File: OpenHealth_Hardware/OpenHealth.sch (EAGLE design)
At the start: 17 parts

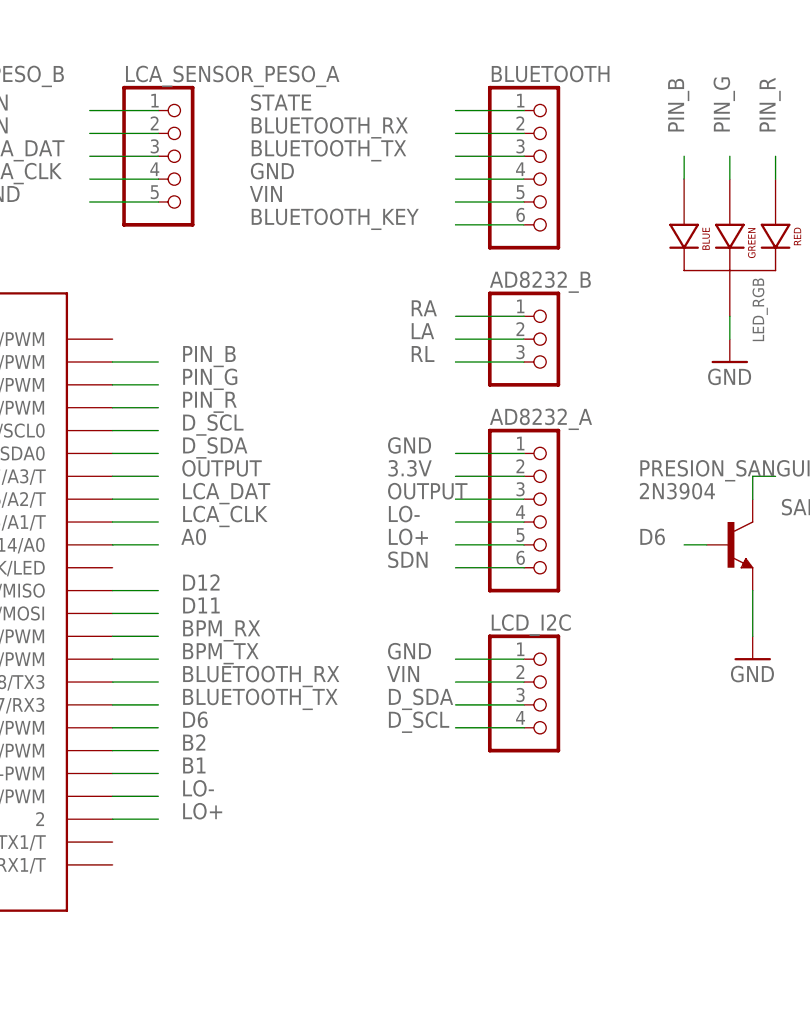
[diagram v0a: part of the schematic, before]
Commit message: Creacion del PCB board y simulacion de los componentes que iran abordo del circuito, PCB board sin enrutar.
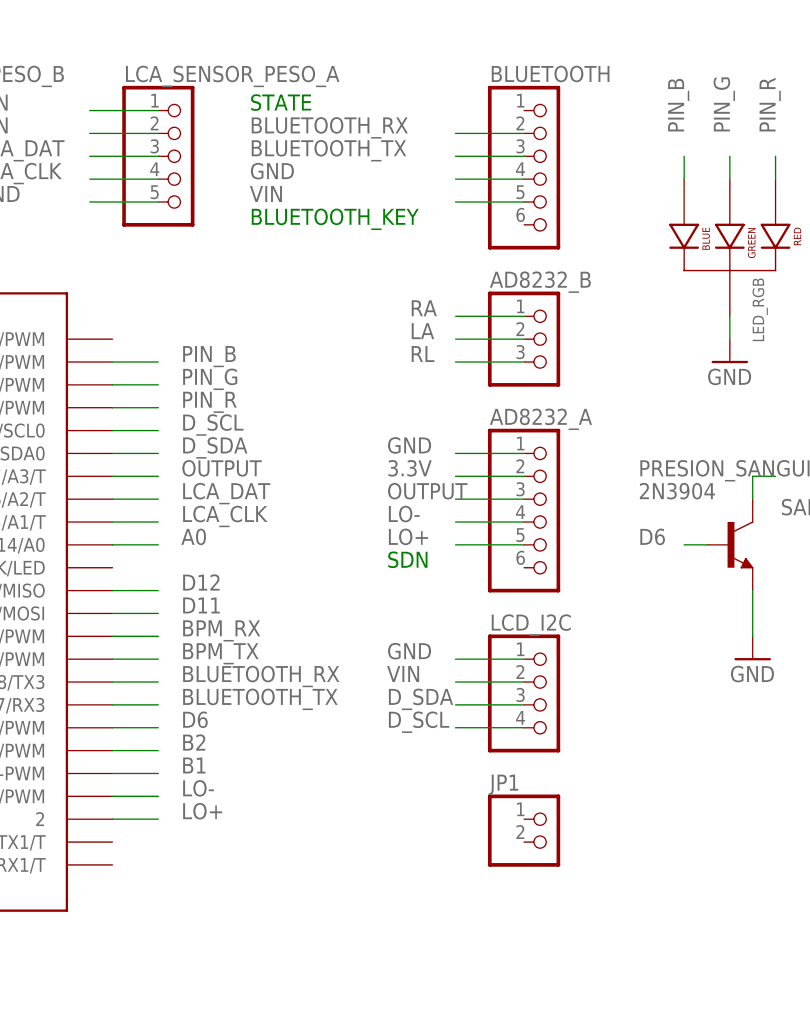
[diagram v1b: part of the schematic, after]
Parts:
- added JP1: (no value), pinhead:PINHD-1X2
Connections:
- removed net BLUETOOTH_KEY: BLUETOOTH.6
- removed net SDN: AD8232_A.6
- removed net STATE: BLUETOOTH.1
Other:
- note added: "BLUETOOTH_KEY"
- note added: "SDN"
- note added: "STATE"
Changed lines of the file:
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@@
 <part name="PRESION_SANGUIENA" library="transistor" deviceset="2N3904" device=""/>
 <part name="GND5" library="supply1" deviceset="GND" device=""/>
+<part name="JP1" library="pinhead" deviceset="PINHD-1X2" device=""/>
 </parts>
 <sheets>
 <sheet>
 <plain>
+<text x="5.08" y="137.16" size="1.778" layer="91">BLUETOOTH_KEY</text>
+<text x="5.08" y="149.86" size="1.778" layer="91">STATE</text>
+<text x="20.32" y="99.06" size="1.778" layer="91">SDN</text>
 </plain>
 <instances>
@@
 <instance part="PRESION_SANGUIENA" gate="G1" x="58.42" y="101.6"/>
 <instance part="GND5" gate="1" x="60.96" y="88.9"/>
+<instance part="JP1" gate="G$1" x="38.1" y="68.58"/>
 </instances>
 <busses>
@@
 </segment>
 </net>
-<net name="SDN" class="0">
-<segment>
-<pinref part="AD8232_A" gate="A" pin="6"/>
-<wire x1="35.56" y1="99.06" x2="27.94" y2="99.06" width="0.1524" layer="91"/>
-<label x="20.32" y="99.06" size="1.778" layer="95"/>
-</segment>
-</net>
 <net name="LO+" class="0">
 <segment>
@@
 </segment>
 </net>
-<net name="BLUETOOTH_KEY" class="0">
-<segment>
-<pinref part="BLUETOOTH" gate="A" pin="6"/>
-<wire x1="35.56" y1="137.16" x2="27.94" y2="137.16" width="0.1524" layer="91"/>
-<label x="5.08" y="137.16" size="1.778" layer="95"/>
-</segment>
-</net>
 <net name="BLUETOOTH_RX" class="0">
 <segment>
@@
 <wire x1="-10.16" y1="86.36" x2="-5.08" y2="86.36" width="0.1524" layer="91"/>
 <label x="-2.54" y="86.36" size="1.778" layer="95"/>
-</segment>
-</net>
-<net name="STATE" class="0">
-<segment>
-<pinref part="BLUETOOTH" gate="A" pin="1"/>
-<wire x1="35.56" y1="149.86" x2="27.94" y2="149.86" width="0.1524" layer="91"/>
-<label x="5.08" y="149.86" size="1.778" layer="95"/>
 </segment>
 </net>
@@
 </sheet>
 </sheets>
+<errors>
+</errors>
 </schematic>
 </drawing>

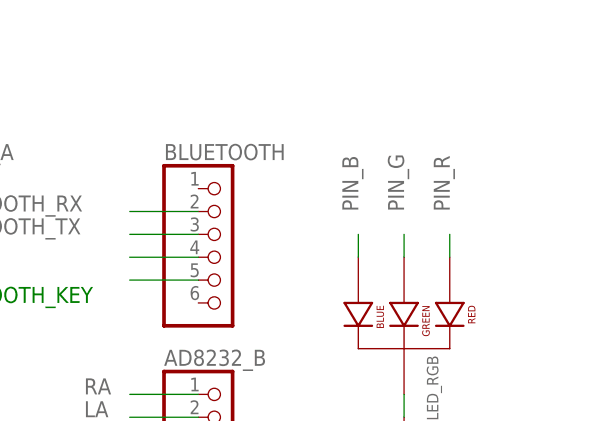
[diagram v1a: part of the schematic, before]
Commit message: Reduccion de la placa madre, se agrego las resistencias faltantes del led y se ordeno previo al enrutado
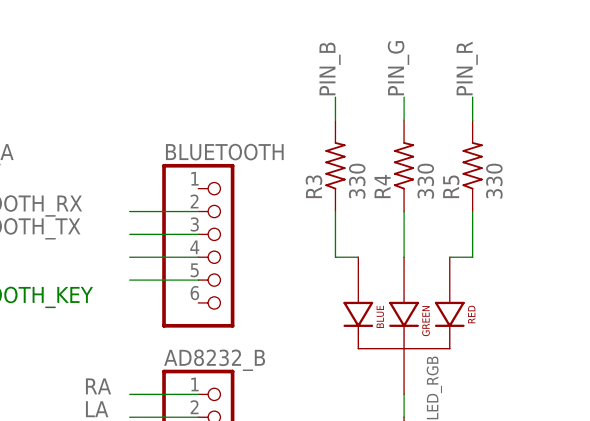
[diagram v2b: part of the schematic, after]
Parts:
- added R3, R4, R5: 330, resistor:R-US_0204/7
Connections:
- new net N$2: LED_RGB.BLUE_CATHODE, R3.1
- new net N$3: LED_RGB.RED_CATHODE, R5.1
- new net N$4: LED_RGB.GREEN_CATHODE, R4.1
- net PIN_B: now also R3.2; no longer LED_RGB.BLUE_CATHODE
- net PIN_G: now also R4.2; no longer LED_RGB.GREEN_CATHODE
- net PIN_R: now also R5.2; no longer LED_RGB.RED_CATHODE
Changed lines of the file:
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@@
 <part name="GND5" library="supply1" deviceset="GND" device=""/>
 <part name="JP1" library="pinhead" deviceset="PINHD-1X2" device=""/>
+<part name="R3" library="resistor" deviceset="R-US_" device="0204/7" value="330"/>
+<part name="R4" library="resistor" deviceset="R-US_" device="0204/7" value="330"/>
+<part name="R5" library="resistor" deviceset="R-US_" device="0204/7" value="330"/>
 </parts>
 <sheets>
@@
 <instance part="GND5" gate="1" x="60.96" y="88.9"/>
 <instance part="JP1" gate="G$1" x="38.1" y="68.58"/>
+<instance part="R3" gate="G$1" x="50.8" y="152.4" rot="R90"/>
+<instance part="R4" gate="G$1" x="58.42" y="152.4" rot="R90"/>
+<instance part="R5" gate="G$1" x="66.04" y="152.4" rot="R90"/>
 </instances>
 <busses>
@@
 <net name="PIN_B" class="0">
 <segment>
-<pinref part="LED_RGB" gate="G$1" pin="BLUE_CATHODE"/>
-<wire x1="53.34" y1="142.24" x2="53.34" y2="144.78" width="0.1524" layer="91"/>
-<label x="53.34" y="147.32" size="1.778" layer="95" rot="R90"/>
-</segment>
-<segment>
 <pinref part="OPENHEALTH" gate="G$1" pin="22/A8/T/PWM"/>
 <wire x1="-10.16" y1="121.92" x2="-5.08" y2="121.92" width="0.1524" layer="91"/>
 <label x="-2.54" y="121.92" size="1.778" layer="95"/>
 </segment>
+<segment>
+<pinref part="R3" gate="G$1" pin="2"/>
+<wire x1="50.8" y1="157.48" x2="50.8" y2="160.02" width="0.1524" layer="91"/>
+<label x="50.8" y="160.02" size="1.778" layer="95" rot="R90"/>
+</segment>
 </net>
 <net name="PIN_G" class="0">
-<segment>
-<pinref part="LED_RGB" gate="G$1" pin="GREEN_CATHODE"/>
-<wire x1="58.42" y1="142.24" x2="58.42" y2="144.78" width="0.1524" layer="91"/>
-<label x="58.42" y="147.32" size="1.778" layer="95" rot="R90"/>
-</segment>
 <segment>
 <pinref part="OPENHEALTH" gate="G$1" pin="21/A7/PWM"/>
@@
 <label x="-2.54" y="119.38" size="1.778" layer="95"/>
 </segment>
+<segment>
+<pinref part="R4" gate="G$1" pin="2"/>
+<wire x1="58.42" y1="157.48" x2="58.42" y2="160.02" width="0.1524" layer="91"/>
+<label x="58.42" y="160.02" size="1.778" layer="95" rot="R90"/>
+</segment>
 </net>
 <net name="PIN_R" class="0">
-<segment>
-<pinref part="LED_RGB" gate="G$1" pin="RED_CATHODE"/>
-<wire x1="63.5" y1="142.24" x2="63.5" y2="144.78" width="0.1524" layer="91"/>
-<label x="63.5" y="147.32" size="1.778" layer="95" rot="R90"/>
-</segment>
 <segment>
 <pinref part="OPENHEALTH" gate="G$1" pin="20/A6/PWM"/>
@@
 <label x="-2.54" y="116.84" size="1.778" layer="95"/>
 </segment>
-</net>
+<segment>
+<pinref part="R5" gate="G$1" pin="2"/>
+<wire x1="66.04" y1="157.48" x2="66.04" y2="160.02" width="0.1524" layer="91"/>
+<label x="66.04" y="160.02" size="1.778" layer="95" rot="R90"/>
+</segment>
+</net>
+<net name="N$2" class="0">
+<segment>
+<pinref part="R3" gate="G$1" pin="1"/>
+<wire x1="50.8" y1="147.32" x2="50.8" y2="142.24" width="0.1524" layer="91"/>
+<pinref part="LED_RGB" gate="G$1" pin="BLUE_CATHODE"/>
+<wire x1="50.8" y1="142.24" x2="53.34" y2="142.24" width="0.1524" layer="91"/>
+</segment>
+</net>
+<net name="N$3" class="0">
+<segment>
+<pinref part="R5" gate="G$1" pin="1"/>
+<wire x1="66.04" y1="147.32" x2="66.04" y2="142.24" width="0.1524" layer="91"/>
+<pinref part="LED_RGB" gate="G$1" pin="RED_CATHODE"/>
+<wire x1="66.04" y1="142.24" x2="63.5" y2="142.24" width="0.1524" layer="91"/>
+</segment>
+</net>
+<net name="N$4" class="0">
+<segment>
+<pinref part="R4" gate="G$1" pin="1"/>
+<pinref part="LED_RGB" gate="G$1" pin="GREEN_CATHODE"/>
+<wire x1="58.42" y1="147.32" x2="58.42" y2="142.24" width="0.1524" layer="91"/>
+</segment>
+</net>
